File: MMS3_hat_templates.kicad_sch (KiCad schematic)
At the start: 6 parts

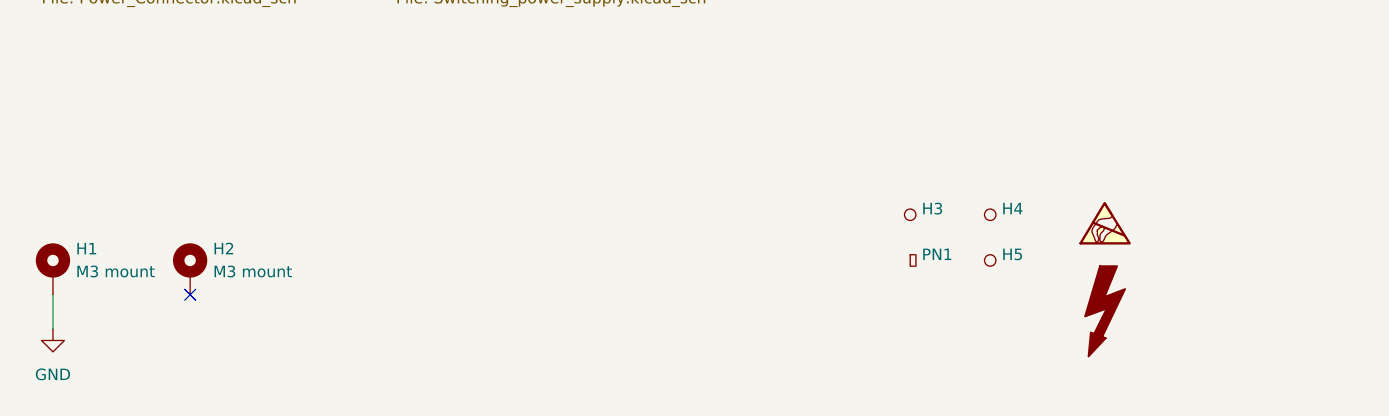
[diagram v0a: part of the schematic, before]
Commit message: Added mechanical standard and updated readme
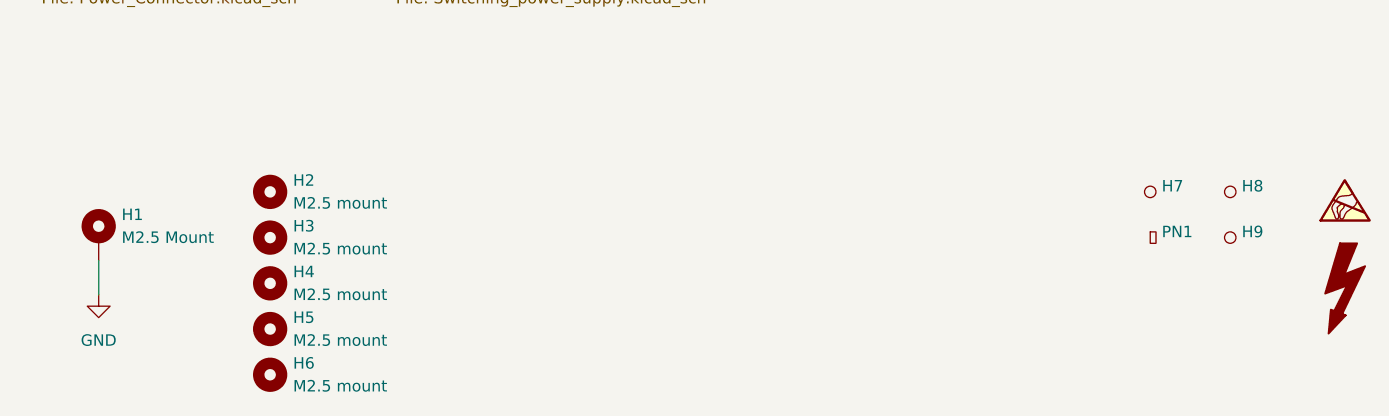
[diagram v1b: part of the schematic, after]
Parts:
- removed H2: M3 mount, MountingHole:MountingHole_3.2mm_M3_DIN965_Pad, symbol Mechanical:MountingHole_Pad
- added H2, H3, H4, H5, H6: M2.5 mount, MountingHole:MountingHole_2.7mm_M2.5, symbol Mechanical:MountingHole
- H1: value M3 mount -> M2.5 Mount; footprint MountingHole:MountingHole_3.2mm_M3_DIN965_Pad -> MountingHole:MountingHole_2.7mm_M2.5_DIN965_Pad_TopOnly
- renumbered H3 to H7, H4 to H8, H5 to H9
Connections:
- no-connect marks 3 -> 2
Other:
- moved on the sheet: H1, H7, H8, H9, PN1

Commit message: moved I2C header to the side
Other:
- company: Moducard System -> MiniModucard System
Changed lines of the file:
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@@
 		(date "2026-02-12")
 		(rev "A")
-		(company "Moducard System")
+		(company "MiniModucard System")
 		(comment 1 "Wojciech Szafrański")
 		(comment 2 "Designed in poland")
